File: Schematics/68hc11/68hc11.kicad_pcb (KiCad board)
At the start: 2 copper layers, 268.6 x 177.2 mm, 37 parts, among them J1 DC 5 Volts, J2 DB9_Female, J3 Screw_Terminal_01x10, J4 Screw_Terminal_01x10, J5 Screw_Terminal_01x10, J6 Screw_Terminal_01x10, SW1 Reset, U1 MC68HC11A1CC-PLLC, U10 MCP100-270D, U2 MC68B21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

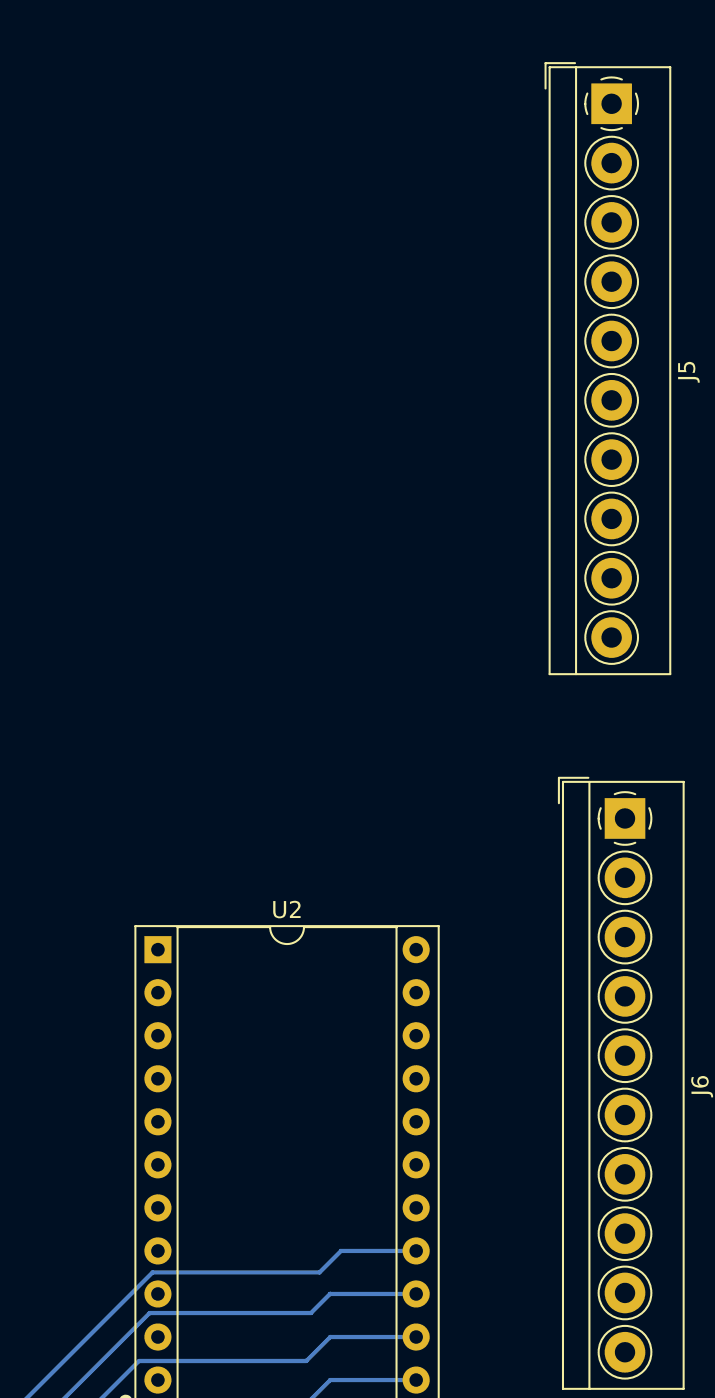
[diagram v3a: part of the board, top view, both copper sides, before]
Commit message: Connected expansion port A
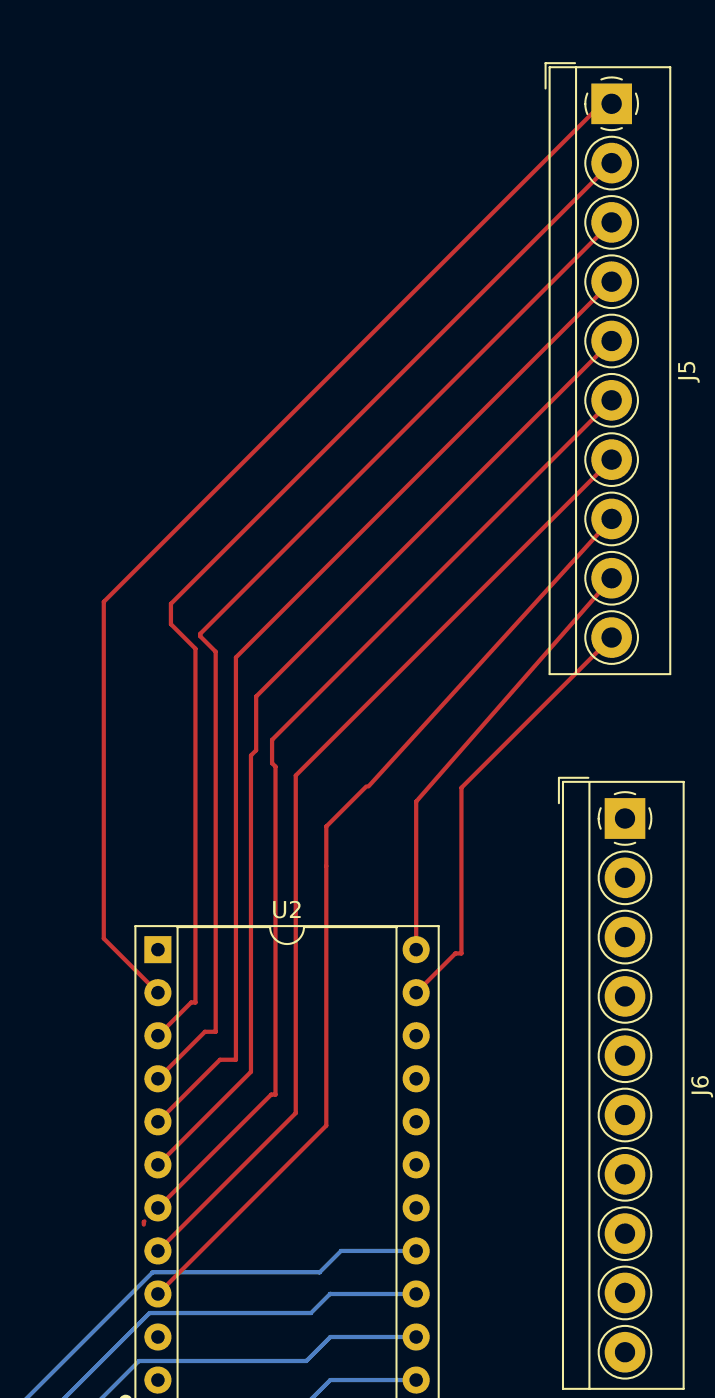
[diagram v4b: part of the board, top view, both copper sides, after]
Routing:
- net /PPA0: track 0.00 -> 66.5 mm
- net /PPA1: track 0.00 -> 63.9 mm
- net /PPA2: track 0.00 -> 62.8 mm
- net /PPA3: track 0.00 -> 61.2 mm
- net /PPA4: track 0.00 -> 59.7 mm
- net /PPA5: track 0.00 -> 59.1 mm
- net /PPA6: track 0.00 -> 57.8 mm
- net /PPA7: track 0.00 -> 56.4 mm
- net /CA1: track 0.00 -> 26.3 mm
- net /CA2: track 0.00 -> 25.9 mm
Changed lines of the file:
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@@
   (gr_line (start 281.305 20.955) (end 281.305 21.59) (layer "Edge.Cuts") (width 0.1))
   (gr_line (start 281.305 21.59) (end 281.305 196.215) (layer "Edge.Cuts") (width 0.1))
+  (segment (start 212.5218 101.1682) (end 212.559505 101.130495) (width 0.25) (layer "F.Cu") (net 0))
+  (segment (start 212.5218 101.3206) (end 212.5218 101.1682) (width 0.25) (layer "F.Cu") (net 0))
   (segment (start 36.13 81.24) (end 33.63 78.74) (width 0.25) (layer "F.Cu") (net 1))
   (segment (start 36.13 88.9) (end 36.13 81.24) (width 0.25) (layer "F.Cu") (net 1))
@@
   (segment (start 27.2422 60.3278) (end 28.3972 60.3278) (width 0.25) (layer "F.Cu") (net 70))
   (segment (start 28.4159 51.9938) (end 27.2609 51.9938) (width 0.25) (layer "F.Cu") (net 70))
+  (segment (start 239.5494 35.177) (end 240.13 35.177) (width 0.25) (layer "F.Cu") (net 76))
+  (segment (start 213.355 87.635) (end 210.1596 84.4396) (width 0.25) (layer "F.Cu") (net 76))
+  (segment (start 210.1596 64.5668) (end 239.5494 35.177) (width 0.25) (layer "F.Cu") (net 76))
+  (segment (start 210.1596 84.4396) (end 210.1596 64.5668) (width 0.25) (layer "F.Cu") (net 76))
+  (segment (start 216.7636 67.5132) (end 215.8492 66.5988) (width 0.25) (layer "F.Cu") (net 77))
+  (segment (start 213.355 92.715) (end 216.1286 89.9414) (width 0.25) (layer "F.Cu") (net 77))
+  (segment (start 216.1286 89.9414) (end 216.7636 89.9414) (width 0.25) (layer "F.Cu") (net 77))
+  (segment (start 216.7636 89.9414) (end 216.7636 67.5132) (width 0.25) (layer "F.Cu") (net 77))
+  (segment (start 215.8492 66.4578) (end 240.13 42.177) (width 0.25) (layer "F.Cu") (net 77))
+  (segment (start 215.8492 66.5988) (end 215.8492 66.4578) (width 0.25) (layer "F.Cu") (net 77))
+  (segment (start 217.0176 91.5924) (end 217.9574 91.5924) (width 0.25) (layer "F.Cu") (net 78))
+  (segment (start 217.9574 91.5924) (end 217.9574 67.8496) (width 0.25) (layer "F.Cu") (net 78))
+  (segment (start 217.9574 67.8496) (end 240.13 45.677) (width 0.25) (layer "F.Cu") (net 78))
+  (segment (start 213.355 95.255) (end 217.0176 91.5924) (width 0.25) (layer "F.Cu") (net 78))
+  (segment (start 218.8464 73.6346) (end 219.1512 73.3298) (width 0.25) (layer "F.Cu") (net 79))
+  (segment (start 213.355 97.795) (end 218.8464 92.3036) (width 0.25) (layer "F.Cu") (net 79))
+  (segment (start 218.8464 92.3036) (end 218.8464 73.6346) (width 0.25) (layer "F.Cu") (net 79))
+  (segment (start 219.1512 70.1558) (end 240.13 49.177) (width 0.25) (layer "F.Cu") (net 79))
+  (segment (start 219.1512 73.3298) (end 219.1512 70.1558) (width 0.25) (layer "F.Cu") (net 79))
+  (segment (start 220.2942 93.6498) (end 220.2942 74.295) (width 0.25) (layer "F.Cu") (net 80))
+  (segment (start 220.091 74.0918) (end 220.091 72.716) (width 0.25) (layer "F.Cu") (net 80))
+  (segment (start 220.091 72.716) (end 240.13 52.677) (width 0.25) (layer "F.Cu") (net 80))
+  (segment (start 220.2942 74.295) (end 220.091 74.0918) (width 0.25) (layer "F.Cu") (net 80))
+  (segment (start 213.355 100.335) (end 220.0402 93.6498) (width 0.25) (layer "F.Cu") (net 80))
+  (segment (start 220.0402 93.6498) (end 220.2942 93.6498) (width 0.25) (layer "F.Cu") (net 80))
+  (segment (start 221.488 74.819) (end 240.13 56.177) (width 0.25) (layer "F.Cu") (net 81))
+  (segment (start 213.355 102.875) (end 221.488 94.742) (width 0.25) (layer "F.Cu") (net 81))
+  (segment (start 221.488 94.742) (end 221.488 74.819) (width 0.25) (layer "F.Cu") (net 81))
+  (segment (start 223.2914 80.1624) (end 223.2914 77.8256) (width 0.25) (layer "F.Cu") (net 82))
+  (segment (start 223.2914 95.4786) (end 223.2914 80.1624) (width 0.25) (layer "F.Cu") (net 82))
+  (segment (start 225.7806 75.4634) (end 240.13 59.677) (width 0.25) (layer "F.Cu") (net 82))
+  (segment (start 223.2914 77.8256) (end 225.6536 75.4634) (width 0.25) (layer "F.Cu") (net 82))
+  (segment (start 213.355 105.415) (end 223.2914 95.4786) (width 0.25) (layer "F.Cu") (net 82))
+  (segment (start 230.9114 85.3186) (end 231.267 85.3186) (width 0.25) (layer "F.Cu") (net 95))
+  (segment (start 228.595 87.635) (end 230.9114 85.3186) (width 0.25) (layer "F.Cu") (net 95))
+  (segment (start 231.267 85.3186) (end 231.267 75.54) (width 0.25) (layer "F.Cu") (net 95))
+  (segment (start 231.267 75.54) (end 240.13 66.677) (width 0.25) (layer "F.Cu") (net 95))
+  (segment (start 228.595 76.3574) (end 240.13 63.177) (width 0.25) (layer "F.Cu") (net 96))
+  (segment (start 228.595 85.095) (end 228.595 76.3574) (width 0.25) (layer "F.Cu") (net 96))
   (segment (start 33.63 88.9) (end 30.28 85.55) (width 0.25) (layer "F.Cu") (net 103))
   (segment (start 33.63 93.32) (end 34.29 93.98) (width 0.25) (layer "F.Cu") (net 103))
@@
   (segment (start 28.3516 115.3362) (end 34.5238 115.3362) (width 0.25) (layer "F.Cu") (net 107))
   (segment (start 18.4256 114.6798) (end 23.2664 119.5206) (width 0.25) (layer "F.Cu") (net 107))
+  (segment (start 214.122 64.685) (end 240.13 38.677) (width 0.25) (layer "F.Cu") (net 115))
+  (segment (start 214.122 65.8876) (end 214.122 64.685) (width 0.25) (layer "F.Cu") (net 115))
+  (segment (start 215.5698 67.3354) (end 214.122 65.8876) (width 0.25) (layer "F.Cu") (net 115))
+  (segment (start 215.5698 88.2142) (end 215.5698 67.3354) (width 0.25) (layer "F.Cu") (net 115))
+  (segment (start 215.3158 88.2142) (end 215.5698 88.2142) (width 0.25) (layer "F.Cu") (net 115))
+  (segment (start 213.355 90.175) (end 215.3158 88.2142) (width 0.25) (layer "F.Cu") (net 115))
   (zone (net 1) (net_name "GND") (layer "B.Cu") (name "Ground") (hatch edge 0.508)
     (connect_pads (clearance 0.508))

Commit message: Still working on traces
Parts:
- moved J4 201.1 mm to (82.3, 37.0), turned to 0 degrees
- moved C5 31.4 mm to (35.7, 126.0)
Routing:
- net /PPB0: track 0.00 -> 42.7 mm
- net /PPB1: track 0.00 -> 42.3 mm
- net /PPB2: track 0.00 -> 41.9 mm
- net /PPB3: track 0.00 -> 40.0 mm
- net /PPB4: track 0.00 -> 39.1 mm
- net /CB2: track 0.00 -> 38.4 mm
- net /PPB5: track 0.00 -> 38.3 mm
- net /PPB6: track 0.00 -> 37.9 mm
- net /CB1: track 0.00 -> 37.7 mm
- net /PPB7: track 0.00 -> 37.5 mm
- net VCC: track 456.0 -> 436.7 mm

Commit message: Updated bad component values
Also generated first Bill Of Materials
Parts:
- C15: value 19 uF -> 10 uF
- R2: value 10 MO -> 10M
- RN1: value 4.7 kO -> 4.7 k
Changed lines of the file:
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@@
       (effects (font (size 1 1) (thickness 0.15)))
     )
-    (fp_text value "10 MO" (at 6.35 2.72) (layer "F.Fab")
+    (fp_text value "10M" (at 6.35 2.72) (layer "F.Fab")
       (effects (font (size 1 1) (thickness 0.15)))
     )
@@
       (effects (font (size 1 1) (thickness 0.15)))
     )
-    (fp_text value "4.7 kO" (at 10.16 2.4) (layer "F.Fab")
+    (fp_text value "4.7 k" (at 10.16 2.4) (layer "F.Fab")
       (effects (font (size 1 1) (thickness 0.15)))
     )
@@
       (effects (font (size 1 1) (thickness 0.15)))
     )
-    (fp_text value "19 uF" (at 1 3.75 90) (layer "F.Fab")
-      (effects (font (size 1 1) (thickness 0.15)))
-    )
+    (fp_text value "10 uF" (at 1 3.75 90) (layer "F.Fab")
+      (effects (font (size 1 1) (thickness 0.15)))
+    )

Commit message: Reset trace routing
Start work on memory address decode logic
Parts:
- moved C5 177.4 mm to (213.0, 133.0)
- moved C4 148.3 mm to (213.0, 143.0)
- moved U1 139.8 mm to (183.0, 99.0)
- moved JP4 129.7 mm to (152.0, 90.0)
- moved RN1 127.8 mm to (163.0, 81.0)
- moved C3 107.6 mm to (198.0, 94.0)
- moved U4 102.5 mm to (164.0, 127.0)
- moved J4 92.7 mm to (159.0, 89.0)
- moved J1 85.4 mm to (23.0, 121.0)
- moved C6 77.2 mm to (213.0, 138.0)
- moved C1 71.3 mm to (23.0, 102.0)
- moved U8 65.9 mm to (117.1, 100.1)
- moved C9 64.6 mm to (122.0, 57.0)
- moved C8 55.9 mm to (213.0, 148.0)
- moved J5 45.7 mm to (200.0, 57.0)
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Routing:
- net VCC: track 436.7 -> 0.00 mm
- net /D3: track 223.6 -> 0.00 mm, vias 2 -> 0
- net /D2: track 216.3 -> 0.00 mm, vias 2 -> 0
- net /D1: track 213.2 -> 0.00 mm, vias 2 -> 0
- net /D0: track 213.1 -> 0.00 mm, vias 2 -> 0
- net /D4: track 212.8 -> 0.00 mm, vias 2 -> 0
- net /D5: track 199.9 -> 0.00 mm, vias 2 -> 0
- net /D6: track 191.8 -> 0.00 mm, vias 2 -> 0
- net /D7: track 185.9 -> 0.00 mm, vias 2 -> 0
- net /AD0: track 163.1 -> 0.00 mm, vias 2 -> 0
- net /AD1: track 152.6 -> 0.00 mm, vias 2 -> 0
- net /AD2: track 147.3 -> 0.00 mm, vias 2 -> 0
- net /A0: track 146.3 -> 0.00 mm
- net /AD4: track 143.4 -> 0.00 mm
- net /A1: track 137.4 -> 0.00 mm
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- removed copper zone on B.Cu, net GND

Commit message: Continueing to rework traces
Addec VCC Plane
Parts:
- moved C6 158.5 mm to (58.2, 103.6)
- moved R2 141.5 mm to (175.4, 91.8)
- moved Y1 140.6 mm to (166.3, 85.8)
- moved C12 134.6 mm to (171.0, 81.3)
- moved C11 126.7 mm to (166.4, 81.0)
- moved U6 86.4 mm to (58.0, 107.0)
- moved JP4 52.0 mm to (201.9, 104.5)
- moved U3 46.6 mm to (138.7, 85.7)
- moved J4 40.6 mm to (162.5, 48.6)
- moved RN1 40.6 mm to (166.5, 40.6)
- moved C2 36.3 mm to (233.9, 104.7)
- moved C3 36.3 mm to (233.9, 99.7)
- moved J3 36.3 mm to (236.9, 119.7)
- moved J5 36.3 mm to (235.9, 62.7)
- moved J6 36.3 mm to (264.9, 82.7)
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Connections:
- U1 pad 51: unconnected-(U1-Pad51) -> /VRL
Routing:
- net /A11: track 0.00 -> 59.2 mm
- net /A9: track 0.00 -> 59.0 mm
- net /A10: track 0.00 -> 56.5 mm
- net /A8: track 0.00 -> 56.1 mm
- net /A12: track 0.00 -> 56.0 mm
- net /D2: track 0.00 -> 52.3 mm
- net /A3: track 0.00 -> 52.3 mm
- net /A2: track 0.00 -> 52.2 mm
- net /A5: track 0.00 -> 52.2 mm
- net /A6: track 0.00 -> 52.2 mm
- net /D6: track 0.00 -> 52.1 mm
- net /A7: track 0.00 -> 52.0 mm
- net /D5: track 0.00 -> 52.0 mm
- net /D7: track 0.00 -> 52.0 mm
- net /D4: track 0.00 -> 52.0 mm
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- added copper zone on B.Cu, net GND
- added copper zone on F.Cu, net VCC
